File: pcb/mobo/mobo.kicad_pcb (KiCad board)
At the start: 2 copper layers, 51.6 x 89 mm, 78 parts, among them J1 SWD_10, J2 PEEL_MOTOR, J3 DRIVE_MOTOR, J5 SPRING_FINGERS, J8 USART1, J9 SWD_10, U1 STM32F031C6Tx, U2 STM32F031K6Ux, U4 AP1117-33, U5 MC34063AD, U6 MAX3078E, U7 DRV8837, U8 DRV8837, Y1 8MHz

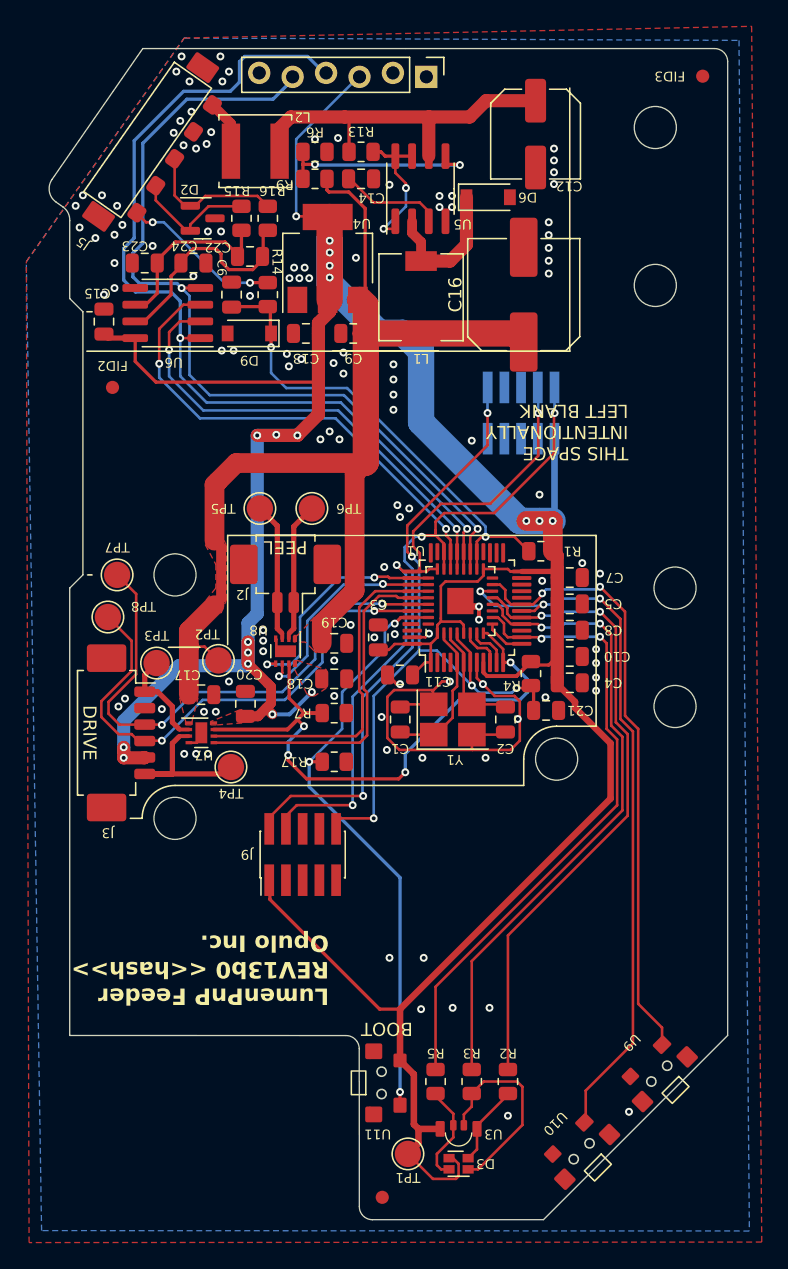
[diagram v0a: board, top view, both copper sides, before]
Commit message: Minor silkscreen and cosmetic fixes
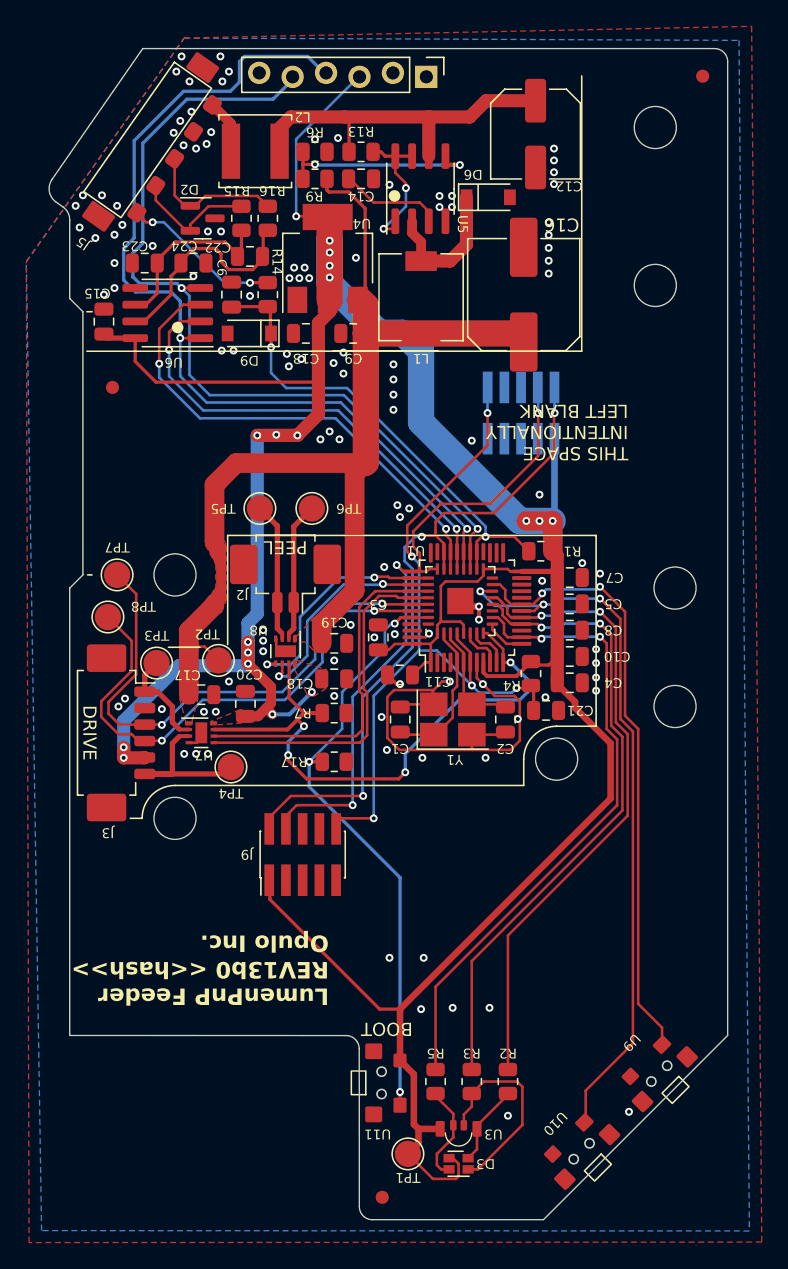
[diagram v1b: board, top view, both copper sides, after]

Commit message: Move a few components to fit inside the power supply compartment
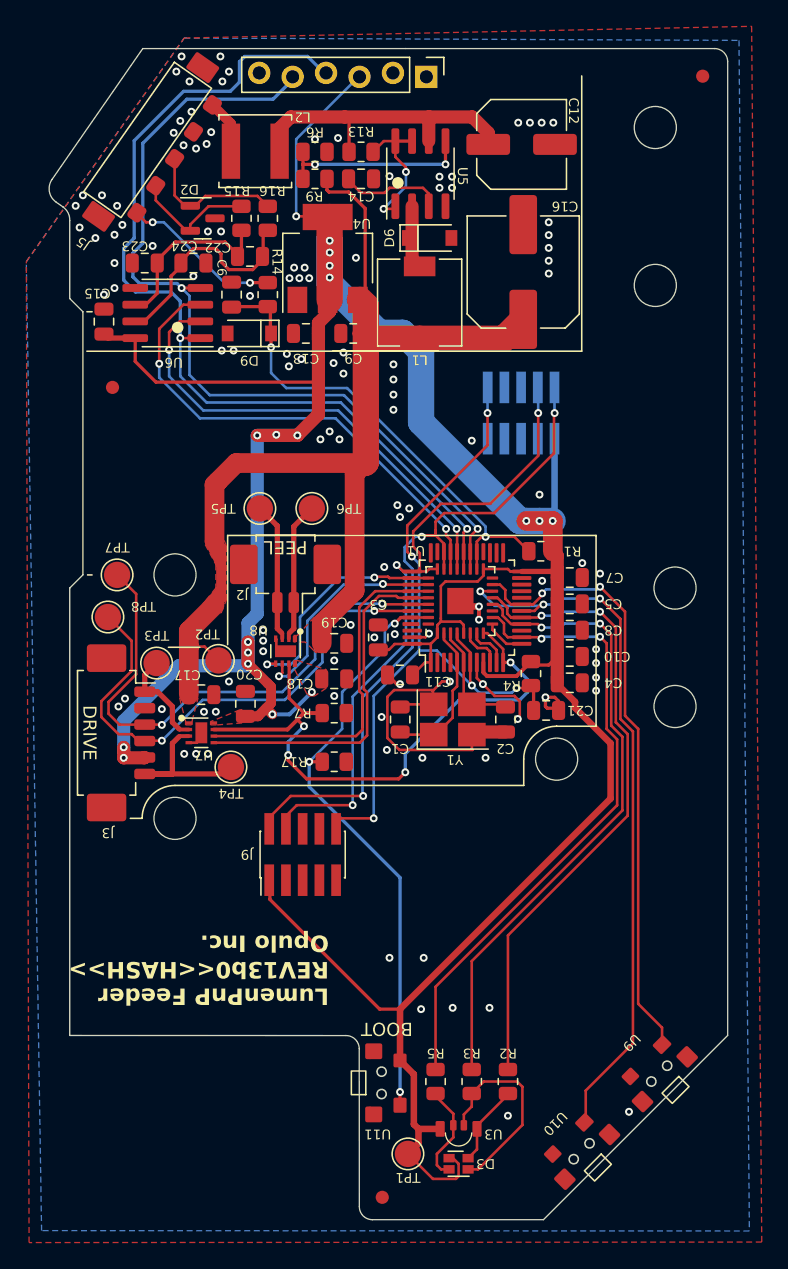
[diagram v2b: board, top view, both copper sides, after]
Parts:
- moved D6 5.42 mm to (128.7, 44.2)
- moved C16 1.72 mm to (135.8, 46.8)
- moved C12 1.32 mm to (135.6, 37.1), turned to 0 degrees
- moved U5 1.14 mm to (128.0, 39.3)
- moved L1 0.42 mm to (127.9, 49.1)
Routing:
- net Net-(D6-K): track 10.9 -> 4.81 mm
- net +VDC: track 27.9 -> 24.0 mm
- net GND: track 43.6 -> 41.5 mm
- net Net-(U5-TC): track 8.47 -> 7.90 mm
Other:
- board text added: "LumenPnP Feeder REV13b0<<HASH>> Opulo Inc."
- board text removed: "LumenPnP Feeder REV13b0 <<hash>> Opulo Inc."
- board text removed: "THIS SPACE INTENTIONALLY LEFT BLANK"
